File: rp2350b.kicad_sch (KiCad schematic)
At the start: 24 parts, among them J2 Conn_01x03_Pin, SW1 Latching, U3 RP2350B_C42415655, U4 W25Q32JVSS, U5 ABM8-272-T3_C20625731

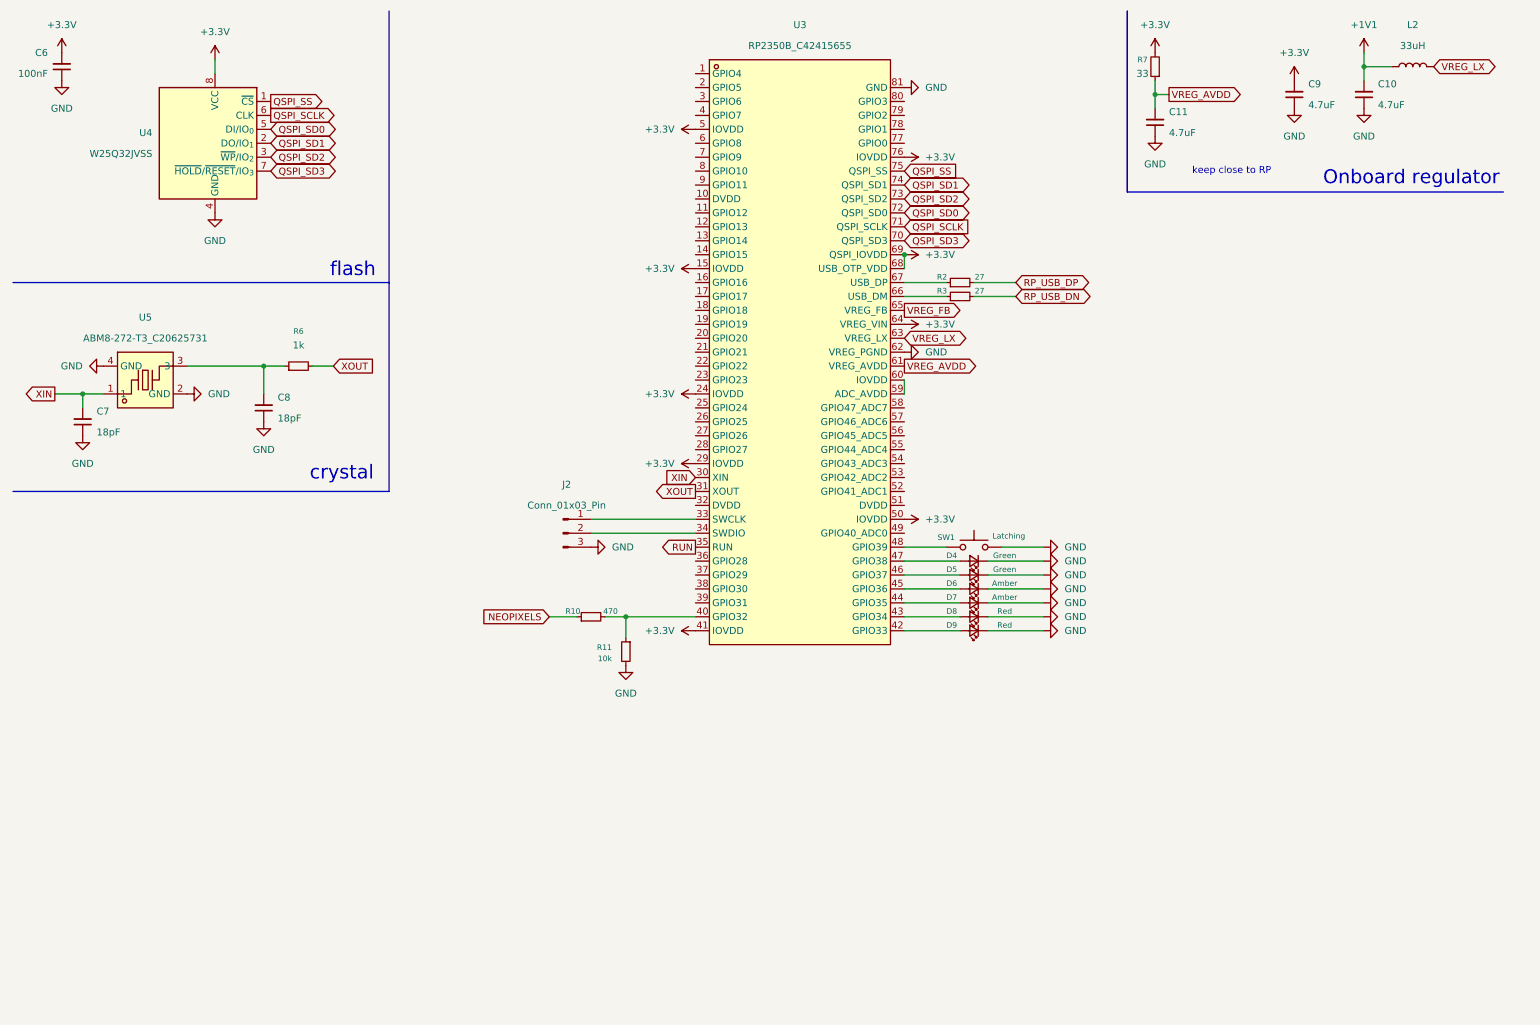
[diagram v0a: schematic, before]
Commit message: gave up on single board, gonna make small modules
Signed-off-by: Toby Cm <toby@vsus.app>
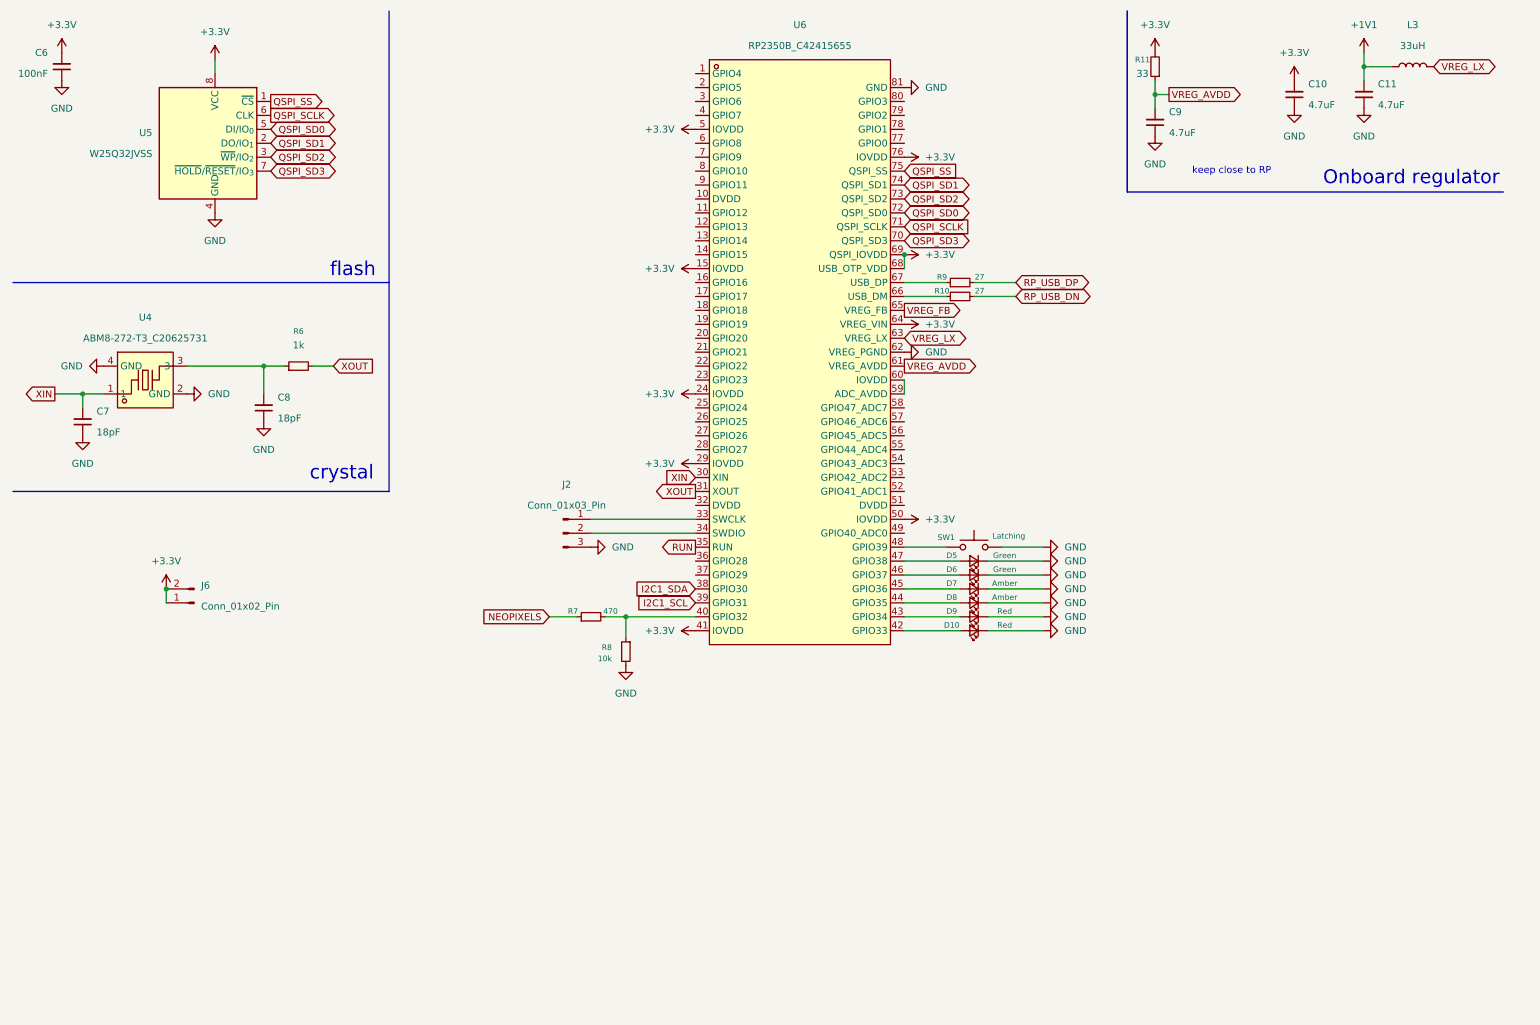
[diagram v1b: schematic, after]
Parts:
- added J6: Conn_01x02_Pin, Connector_PinHeader_2.54mm:PinHeader_1x02_P2.54mm_Vertical, symbol Connector:Conn_01x02_Pin
- C10: renamed from C9; footprint (none) -> Capacitor_SMD:C_0603_1608Metric_Pad1.08x0.95mm_HandSolder
- C11: renamed from C10; footprint (none) -> Capacitor_SMD:C_0603_1608Metric_Pad1.08x0.95mm_HandSolder
- C6, C7, C8: footprint (none) -> Capacitor_SMD:C_0201_0603Metric_Pad0.64x0.40mm_HandSolder
- C9: renamed from C11; footprint (none) -> Capacitor_SMD:C_0603_1608Metric_Pad1.08x0.95mm_HandSolder
- D10: renamed from D9; footprint (none) -> LED_SMD:LED_0603_1608Metric_Pad1.05x0.95mm_HandSolder
- D5: renamed from D4; footprint (none) -> LED_SMD:LED_0603_1608Metric_Pad1.05x0.95mm_HandSolder
- D6: renamed from D5; footprint (none) -> LED_SMD:LED_0603_1608Metric_Pad1.05x0.95mm_HandSolder
- D7: renamed from D6; footprint (none) -> LED_SMD:LED_0603_1608Metric_Pad1.05x0.95mm_HandSolder
- D8: renamed from D7; footprint (none) -> LED_SMD:LED_0603_1608Metric_Pad1.05x0.95mm_HandSolder
- D9: renamed from D8; footprint (none) -> LED_SMD:LED_0603_1608Metric_Pad1.05x0.95mm_HandSolder
- J2: footprint (none) -> Connector_PinHeader_2.54mm:PinHeader_1x03_P2.54mm_Vertical
- R10: renamed from R3; footprint (none) -> Resistor_SMD:R_0402_1005Metric_Pad0.72x0.64mm_HandSolder
- R11: renamed from R7; footprint (none) -> Resistor_SMD:R_0402_1005Metric_Pad0.72x0.64mm_HandSolder
- R6: footprint (none) -> Resistor_SMD:R_0402_1005Metric_Pad0.72x0.64mm_HandSolder
- R7: renamed from R10; footprint (none) -> Resistor_SMD:R_0402_1005Metric_Pad0.72x0.64mm_HandSolder
- R8: renamed from R11; footprint (none) -> Resistor_SMD:R_0402_1005Metric_Pad0.72x0.64mm_HandSolder
- R9: renamed from R2; footprint (none) -> Resistor_SMD:R_0402_1005Metric_Pad0.72x0.64mm_HandSolder
- SW1: footprint (none) -> easyeda2kicad:SW-TH_6P-L8.0-W8.0-P2.50
- renumbered L2 to L3, U5 to U4, U4 to U5, U3 to U6
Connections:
- net +3.3V: now also J6.1 (Pin_1), J6.2 (Pin_2)
- net I2C1_SDA: now reaches U6.38 (GPIO30)
- net I2C1_SCL: now reaches U6.39 (GPIO31)

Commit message: updated journal, pin headers footprint, etc. added labels to rp2350b, finished pcb routing. time to start on other modules yay
Signed-off-by: Toby Cm <toby@vsus.app>
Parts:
- removed J2: Conn_01x03_Pin, Connector_PinHeader_2.54mm:PinHeader_1x03_P2.54mm_Vertical, symbol Connector:Conn_01x03_Pin
- removed J6: Conn_01x02_Pin, Connector_PinHeader_2.54mm:PinHeader_1x02_P2.54mm_Vertical, symbol Connector:Conn_01x02_Pin
- removed L3: 33uH, symbol Device:L
- added C16, C17, C18, C19, C20, C21, C22, C23: 100nF, Capacitor_SMD:C_0201_0603Metric_Pad0.64x0.40mm_HandSolder, symbol Device:C_Small
- added J20, J23: Conn_01x02_Pin, Connector_PinHeader_2.54mm:PinHeader_1x02_P2.54mm_Vertical, symbol Connector:Conn_01x02_Pin
- added J21: Conn_01x04_Pin, Connector_PinHeader_2.54mm:PinHeader_2x02_P2.54mm_Vertical, symbol Connector:Conn_01x04_Pin
- added J3, J4, J7: Conn_01x10_Pin, Connector_PinHeader_2.54mm:PinHeader_1x10_P2.54mm_Vertical, symbol Connector:Conn_01x10_Pin
- added L1: AOTA-B201610S3R3-101-T, easyeda2kicad:IND-SMD_L2.0-W1.6_AOTA-B201610S3R3-101-T, symbol easyeda2kicad:AOTA-B201610S3R3-101-T
- added R14, R15: 1k, Resistor_SMD:R_0402_1005Metric_Pad0.72x0.64mm_HandSolder, symbol Device:R_Small
- added SW2, SW3, SW4: TS24CA, easyeda2kicad:SW-SMD_TS24CA, symbol easyeda2kicad:TS24CA
- renumbered C6 to C3, C10 to C4, C11 to C5, C9 to C6, C8 to C7, C7 to C8, D5 to D2, D6 to D3, D7 to D4, D8 to D5, D9 to D6, D10 to D7, R11 to R2, R9 to R3, R10 to R4, R6 to R5, R7 to R6, R8 to R7, U5 to U1, U6 to U2, U4 to U3
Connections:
- net +1V1: now also U2.10 (DVDD), U2.32 (DVDD), U2.51 (DVDD), J20.1 (Pin_1), J20.2 (Pin_2), L1.1
- net +3.3V: now also U2.59 (ADC_AVDD), U2.60 (IOVDD), C16.2, C17.2, C18.2, C19.2, C20.2, C21.2, C22.2, C23.2, J21.1 (Pin_1), J21.2 (Pin_2), J21.3 (Pin_3), J21.4 (Pin_4)
- net GND: now also C16.1, C17.1, C18.1, C19.1, C20.1, C21.1, C22.1, C23.1, J3.3 (Pin_3), J3.8 (Pin_8), J4.3 (Pin_3), J4.8 (Pin_8), J7.3 (Pin_3), J7.8 (Pin_8), R14.1, R15.1, SW2.1, SW2.2, SW3.1, SW3.2, SW4.1, SW4.2, SW4.3
- net QSPI_SS: now also SW2.4
- net RP_USB_DN: now also J23.1 (Pin_1)
- net RP_USB_DP: now also J23.2 (Pin_2)
- net RUN: now also SW3.4
- net VREG_LX: now also L1.2
- net at R6.2, R7.1: no longer U2.40 (GPIO32)
- net GPIO4: now reaches U2.1 (GPIO4)
- net GPIO4: now also J3.6 (Pin_6)
- net GPIO12: now reaches U2.11 (GPIO12)
- net GPIO12: now also J4.6 (Pin_6)
- net GPIO13: now reaches U2.12 (GPIO13)
- net GPIO13: now also J4.7 (Pin_7)
- net GPIO14: now reaches U2.13 (GPIO14)
- net GPIO14: now also J4.9 (Pin_9)
- net GPIO15: now reaches U2.14 (GPIO15)
- net GPIO15: now also J4.10 (Pin_10)
- net GPIO16: now reaches U2.16 (GPIO16)
- net GPIO17: now reaches U2.17 (GPIO17)
- net GPIO18: now reaches U2.18 (GPIO18)
- net GPIO19: now reaches U2.19 (GPIO19)
- net GPIO5: now reaches U2.2 (GPIO5)
- net GPIO5: now also J3.7 (Pin_7)
- net GPIO20: now reaches U2.20 (GPIO20)
- net GPIO21: now reaches U2.21 (GPIO21)
- net GPIO22: now reaches U2.22 (GPIO22)
- net GPIO23: now reaches U2.23 (GPIO23)
- net GPIO24: now reaches U2.25 (GPIO24)
- net GPIO25: now reaches U2.26 (GPIO25)
- net GPIO26: now reaches U2.27 (GPIO26)
- net GPIO27: now reaches U2.28 (GPIO27)
- net GPIO6: now reaches U2.3 (GPIO6)
- net GPIO6: now also J3.9 (Pin_9)
- net SWCLK: now reaches U2.33 (SWCLK)
- net SWDIO: now reaches U2.34 (SWDIO)
- net GPIO28: now reaches U2.36 (GPIO28)
- net GPIO29: now reaches U2.37 (GPIO29)
- net GPIO7: now reaches U2.4 (GPIO7)
- net GPIO7: now also J3.10 (Pin_10)
- net GPIO40: now reaches U2.49 (GPIO40_ADC0)
- net GPIO40: now also J7.1 (Pin_1)
- net GPIO41: now reaches U2.52 (GPIO41_ADC1)
- net GPIO41: now also J7.2 (Pin_2)
- net GPIO42: now reaches U2.53 (GPIO42_ADC2)
- net GPIO42: now also J7.4 (Pin_4)
- net GPIO43: now reaches U2.54 (GPIO43_ADC3)
- net GPIO43: now also J7.5 (Pin_5)
- net GPIO44: now reaches U2.55 (GPIO44_ADC4)
- net GPIO44: now also J7.6 (Pin_6)
- net GPIO45: now reaches U2.56 (GPIO45_ADC5)
- net GPIO45: now also J7.7 (Pin_7)
- net GPIO46: now reaches U2.57 (GPIO46_ADC6)
- net GPIO46: now also J7.9 (Pin_9)
- net GPIO47: now reaches U2.58 (GPIO47_ADC7)
- net GPIO47: now also J7.10 (Pin_10)
- net GPIO8: now reaches U2.6 (GPIO8)
- net GPIO8: now also J4.1 (Pin_1)
- net GPIO9: now reaches U2.7 (GPIO9)
- net GPIO9: now also J4.2 (Pin_2)
- net GPIO0: now reaches U2.77 (GPIO0)
- net GPIO0: now also J3.1 (Pin_1)
- net GPIO1: now reaches U2.78 (GPIO1)
- net GPIO1: now also J3.2 (Pin_2)
- net GPIO2: now reaches U2.79 (GPIO2)
- net GPIO2: now also J3.4 (Pin_4)
- net GPIO10: now reaches U2.8 (GPIO10)
- net GPIO10: now also J4.4 (Pin_4)
- net GPIO3: now reaches U2.80 (GPIO3)
- net GPIO3: now also J3.5 (Pin_5)
- net GPIO11: now reaches U2.9 (GPIO11)
- net GPIO11: now also J4.5 (Pin_5)
- net I2C1_SCL renamed GPIO31
- net I2C1_SDA renamed GPIO30
- new net: SW4.4, U2.40 (GPIO32)
- new net: R15.2, SW3.3
- new net: R14.2, SW2.3
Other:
- note added: "BOOTSEL button"
- note added: "RUN button"
- moved on the sheet: C4, C5, C6, R2, R6, R7, SW1
